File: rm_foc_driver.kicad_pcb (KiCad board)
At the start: 4 copper layers, 70 x 70 mm, 78 parts, among them J1 SWD, J2 TMC4671, J3 UART, J4 TMC4671, J6 Conn_01x02, J8 Conn_01x03, Q1 CSD18540Q5B, Q2 CSD18540Q5B, Q3 CSD18540Q5B, Q4 CSD18540Q5B, Q5 CSD18540Q5B, Q6 CSD18540Q5B, U1 TPS54540, U10 74HC244, U2 RT9013, U3 STM32F401CCUx, U4 AMS1117-5.0, U5 IR2104, U6 INA2180, U7 MT6701, U8 IR2104, U9 IR2104, Y1 Crystal_GND24

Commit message: version 1.1.0-beta
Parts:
- added C19: 47uF, Capacitor_SMD:C_0805_2012Metric, F.Cu at (190.5, 97.0)
- added C20: 1uF, Capacitor_SMD:C_0603_1608Metric, F.Cu at (186.4, 96.9)
- added C21: 1uF, Capacitor_SMD:C_0603_1608Metric, F.Cu at (137.4, 104.4)
- added C23: 47uF, Capacitor_SMD:C_0805_2012Metric, F.Cu at (189.1, 105.7)
- added J5: Conn_01x03, Connector_PinSocket_2.54mm:PinSocket_1x03_P2.54mm_Vertical, F.Cu at (140.2, 121.9)
- added L2: 2.2uH, Inductor_SMD:L_Neosid_Ms42, F.Cu at (183.4, 102.9)
- added R17: 190k, Resistor_SMD:R_0603_1608Metric, F.Cu at (194.7, 103.1)
- added R18: 10k, Resistor_SMD:R_0603_1608Metric, F.Cu at (196.7, 99.5)
- added R19: 10k, Resistor_SMD:R_0603_1608Metric, F.Cu at (194.7, 99.5)
- added R20: 105k, Resistor_SMD:R_0603_1608Metric, F.Cu at (196.7, 103.1)
- C1: value 1uF -> 10nF
- L1: footprint Inductor_SMD:L_7.3x7.3_H4.5 -> Inductor_SMD:L_Neosid_Ms42
- U4: value AMS1117-5.0 -> SY8303; footprint Package_TO_SOT_SMD:SOT-223-3_TabPin2 -> Package_TO_SOT_SMD:TSOT-23-8
- moved C15 31.2 mm to (154.2, 113.3)
- moved U6 30.2 mm to (149.1, 113.5)
- moved C2 18.9 mm to (178.3, 97.0), turned to -90 degrees
- moved R13 16.5 mm to (160.0, 94.5)
- moved R10 16.5 mm to (158.8, 83.4)
- moved Q5 16.3 mm to (145.3, 87.1)
- moved Q6 16.3 mm to (145.5, 79.5)
- moved Q1 16.1 mm to (161.5, 87.1)
- moved Q2 16.1 mm to (161.8, 79.5)
- moved C18 15.1 mm to (143.9, 94.5)
- moved U8 14.0 mm to (160.0, 101.6)
- moved R16 13.8 mm to (148.0, 94.5)
- moved R14 13.7 mm to (162.1, 94.5)
- moved U9 13.5 mm to (146.1, 101.6)
- moved C17 12.7 mm to (158.0, 94.5)
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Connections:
- C1 pad 1: +12V -> Net-(C1-Pad1)
- C1 pad 2: GND -> Net-(C1-Pad2)
- J4 pad 4: /CS2 -> /CS1
- J8 pad 1: /SH_C -> /SH_A
- J8 pad 3: /SH_A -> /SH_C
- U3 pad 14: /CS2 -> /CS1
- U4 pad 1: GND -> Net-(R17-Pad2)
- U4 pad 2: +5V -> Net-(R19-Pad1)
- U4 pad 3: +12V -> GND
- U7 pad 2: /MODE -> +5V
- U7 pad 3: /ADC1 -> unconnected-(U7-Pad3)
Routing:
- net /MODE: track 67.4 -> 0.00 mm, vias 1 -> 0
- net /ADC1: track 35.7 -> 0.00 mm, vias 2 -> 0
- net /CS1: track 33.3 -> 69.0 mm
- net Net-(C18-Pad1): track 13.2 -> 34.0 mm
- net Net-(C17-Pad1): track 33.1 -> 13.1 mm
- net /PWMA: track 28.3 -> 8.46 mm
- net /SL_A: track 66.8 -> 49.6 mm
- net /PWMC: track 8.39 -> 23.5 mm
- net /CS2: track 14.6 -> 0.00 mm
- net GND: track 21.5 -> 7.71 mm, vias 129 -> 37
- net /SO1: track 47.1 -> 35.0 mm, vias 2 -> 1
- net +3.3V: track 116.6 -> 106.9 mm, vias 7 -> 14
- net Net-(R20-Pad2): track 0.00 -> 8.41 mm
- net /SWDIO: track 25.0 -> 16.6 mm
- net /SO2: track 48.5 -> 40.4 mm, vias 2 -> 1
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- added copper zone on B.Cu, net +12V
- added copper zone on F.Cu, net +12V
- added copper zone on In1.Cu, net +12V
- added copper zone on In2.Cu, net +12V
- added copper zone on B.Cu, net +24V
- added copper zone on B.Cu, net +3.3V
- added copper zone on F.Cu, net +3.3V
- added copper zone on In1.Cu, net +3.3V
- added copper zone on In2.Cu, net +3.3V
- added copper zone on B.Cu, net +5V
- added copper zone on F.Cu, net +5V
- added copper zone on In1.Cu, net +5V
- added copper zone on In2.Cu, net +5V
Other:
- board text added: "A"
- board text added: "B"
- board text added: "Z"
- board text removed: "2022/10/3"
- board text removed: "CLK"
- board text removed: "CS2"
- board text removed: "DynamicX"
- board text removed: "MISO"
- board text removed: "MOSI"
- board text removed: "Q2"
- board text removed: "VER3.0"
- board text removed: "cyl0411"

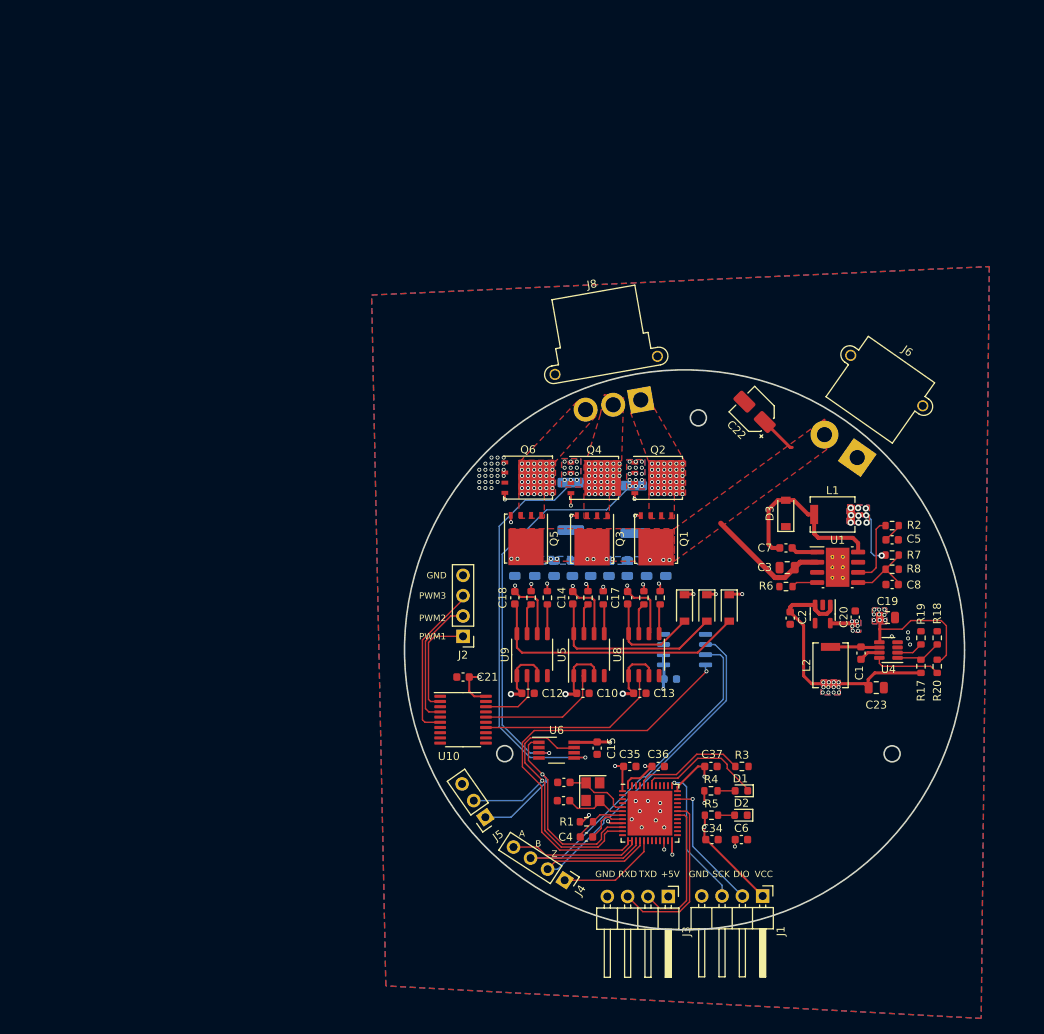
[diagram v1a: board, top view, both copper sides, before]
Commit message: remove mcu...
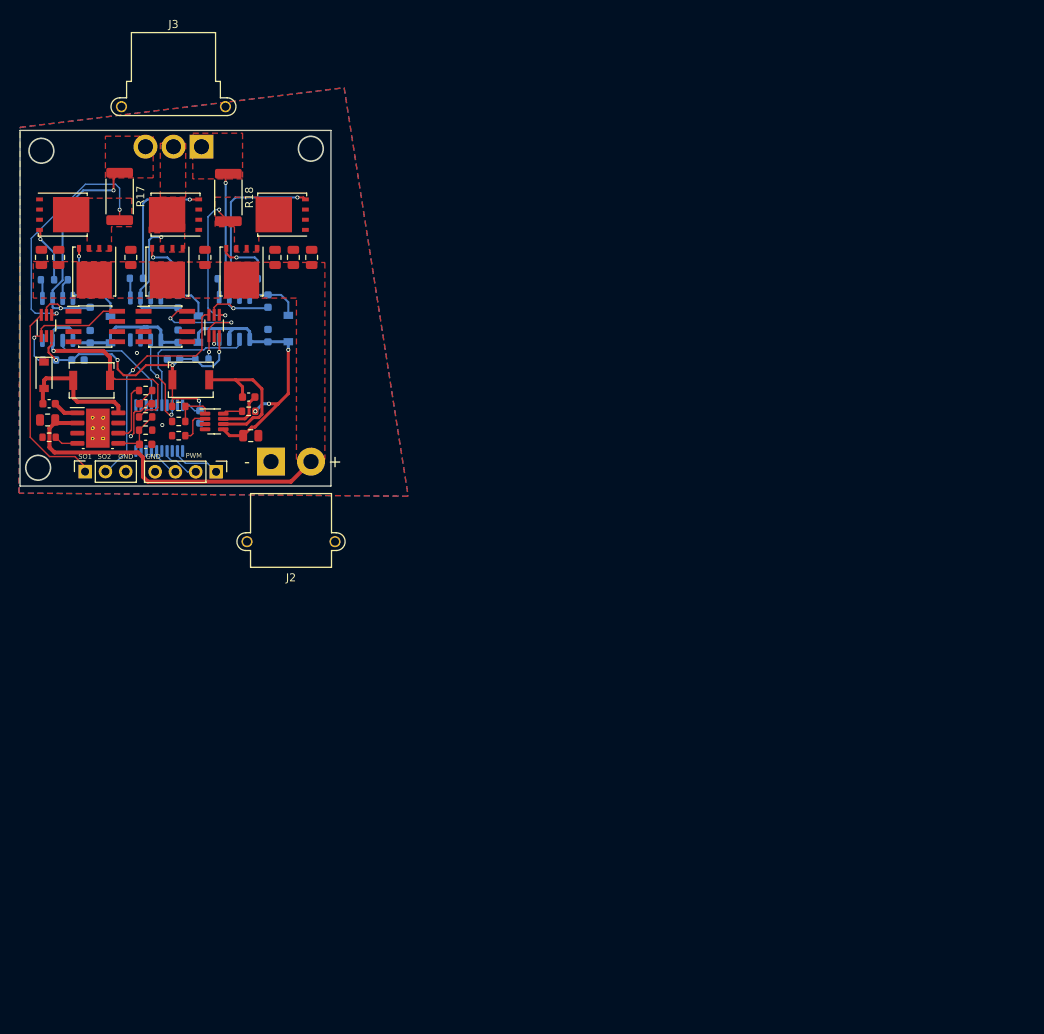
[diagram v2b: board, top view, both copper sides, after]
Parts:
- removed C15: 1uF, Capacitor_SMD:C_0603_1608Metric
- removed C24, C25, C26, C27, C29, C30, C31, C32, C33: 10uF, Capacitor_SMD:C_0805_2012Metric
- removed C34, C35, C36, C37: 100nF, Capacitor_SMD:C_0603_1608Metric
- removed D5, D6: DIODE, Diode_SMD:D_SOD-123
- removed J5: Conn_01x03, Connector_PinSocket_2.54mm:PinSocket_1x03_P2.54mm_Vertical
- removed J6: Conn_01x02, Connector_AMASS:AMASS_XT30PW-M_1x02_P2.50mm_Horizontal
- removed J8: Conn_01x03, Connector_AMASS:AMASS_MR30PW-FB_1x03_P3.50mm_Horizontal
- removed R19: 10k, Resistor_SMD:R_0603_1608Metric
- removed R20: 105k, Resistor_SMD:R_0603_1608Metric
- removed Y1: Crystal_GND24, Crystal:Crystal_SMD_3225-4Pin_3.2x2.5mm
- C1: value 10nF -> 10uF; footprint Capacitor_SMD:C_0603_1608Metric -> Capacitor_SMD:C_0805_2012Metric
- C10, C12, C13, C8, D3, D4, R12, R13, R14, R15, R16, U10, U5: moved to B.Cu
- C11, C9: value 22pF -> 100nF; moved to B.Cu
- C14: value 100nF -> 1uF; moved to B.Cu
- C16: value 1uF -> 10uF; footprint Capacitor_SMD:C_0603_1608Metric -> Capacitor_SMD:C_0805_2012Metric; moved to F.Cu
- C17, C18: value 100nF -> 10uF; footprint Capacitor_SMD:C_0603_1608Metric -> Capacitor_SMD:C_0805_2012Metric
- C19: value 47uF -> 10uF
- C2: value 1uF -> 100nF; moved to B.Cu
- C20, C21: value 1uF -> 10uF; footprint Capacitor_SMD:C_0603_1608Metric -> Capacitor_SMD:C_0805_2012Metric
- C22: value C_Polarized -> 10uF; footprint Capacitor_SMD:CP_Elec_4x5.4 -> Capacitor_SMD:C_0805_2012Metric
- C23: value 47uF -> 100nF; footprint Capacitor_SMD:C_0805_2012Metric -> Capacitor_SMD:C_0603_1608Metric; moved to B.Cu
- C3: value 10uF -> 6.8nF; footprint Capacitor_SMD:C_0805_2012Metric -> Capacitor_SMD:C_0603_1608Metric
- C4: value 100nF -> 10nF
- C5: value 6.8nF -> 100nF
- C6: value 4.7uF -> 47uF; footprint Capacitor_SMD:C_0603_1608Metric -> Capacitor_SMD:C_0805_2012Metric
- D1: value LED -> DIODE; footprint LED_SMD:LED_0603_1608Metric -> Diode_SMD:D_SOD-123
- D2: value LED -> DIODE; footprint LED_SMD:LED_0603_1608Metric -> Diode_SMD:D_SOD-123; moved to B.Cu
- J1: value SWD -> TMC4671; footprint Connector_PinHeader_2.54mm:PinHeader_1x04_P2.54mm_Horizontal -> Connector_PinHeader_2.54mm:PinHeader_1x04_P2.54mm_Vertical
- J2: value TMC4671 -> Conn_01x02; footprint Connector_PinHeader_2.54mm:PinHeader_1x04_P2.54mm_Vertical -> Connector_AMASS:AMASS_XT30PW-M_1x02_P2.50mm_Horizontal
- J3: value UART -> Conn_01x03; footprint Connector_PinHeader_2.54mm:PinHeader_1x04_P2.54mm_Horizontal -> Connector_AMASS:AMASS_MR30PW-FB_1x03_P3.50mm_Horizontal
- J4: value TMC4671 -> Conn_01x03; footprint Connector_PinHeader_2.54mm:PinHeader_1x04_P2.54mm_Vertical -> Connector_PinSocket_2.54mm:PinSocket_1x03_P2.54mm_Vertical
- L1: value 6.5uH -> 2.2uH
- L2: value 2.2uH -> 6.5uH
- R1: value 10k -> 25k
- R10: value 0.01R -> 2.5k; footprint Resistor_SMD:R_2512_6332Metric -> Resistor_SMD:R_0603_1608Metric
- R11: value 0.01R -> 20R; footprint Resistor_SMD:R_2512_6332Metric -> Resistor_SMD:R_0603_1608Metric
- R17: value 190k -> 0.01R; footprint Resistor_SMD:R_0603_1608Metric -> Resistor_SMD:R_2512_6332Metric
- R18: value 10k -> 0.01R; footprint Resistor_SMD:R_0603_1608Metric -> Resistor_SMD:R_2512_6332Metric
- R2: value 25k -> 190k
- R4: value 10k -> 225k
- R6: value 225k -> 105k
- R9: value 20R -> 2.5k; moved to B.Cu
- U2: value RT9013 -> SY8303; footprint Package_TO_SOT_SMD:SOT-23-5 -> Package_TO_SOT_SMD:TSOT-23-8
- U3: value STM32F401CCUx -> IR2104; footprint Package_DFN_QFN:QFN-48-1EP_7x7mm_P0.5mm_EP5.6x5.6mm -> Package_SO:SOP-8_3.9x4.9mm_P1.27mm; moved to B.Cu
- U4: value SY8303 -> IR2104; footprint Package_TO_SOT_SMD:TSOT-23-8 -> Package_SO:SOP-8_3.9x4.9mm_P1.27mm; moved to B.Cu
- U6: value INA2180 -> LM236; footprint Package_SO:VSSOP-8_3.0x3.0mm_P0.65mm -> Package_SO:PowerIntegrations_SO-8
- U7: value MT6701 -> LM236; footprint Package_SO:SOP-8_3.9x4.9mm_P1.27mm -> Package_SO:PowerIntegrations_SO-8; moved to F.Cu
- U8, U9: value IR2104 -> INA199; footprint Package_SO:SOP-8_3.9x4.9mm_P1.27mm -> Package_TO_SOT_SMD:SOT-363_SC-70-6_Handsoldering
- moved R17 116.1 mm to (94.5, 44.3), turned to -90 degrees
- moved U4 111.8 mm to (86.7, 59.7), turned to 90 degrees
- moved J3 110.4 mm to (104.7, 38.1), turned to 0 degrees
- moved C23 107.9 mm to (89.3, 64.8)
- moved C5 106.7 mm to (85.7, 70.2), turned to 180 degrees
- moved C1 105.8 mm to (85.5, 72.3), turned to 180 degrees
- moved R18 104.3 mm to (108.1, 44.5), turned to -90 degrees
- moved D1 101.5 mm to (85.0, 66.7), turned to -90 degrees
- moved L2 99.0 mm to (91.0, 67.3), turned to 0 degrees
- moved C19 96.5 mm to (105.2, 51.9), turned to 90 degrees
- moved R8 94.9 mm to (97.7, 73.5)
- moved R7 94.9 mm to (97.7, 71.9)
- moved U1 94.1 mm to (91.8, 73.3)
- moved R4 93.8 mm to (85.7, 74.4), turned to 180 degrees
- moved C16 92.9 mm to (86.9, 51.9), turned to 90 degrees
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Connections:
- C1 pad 1: Net-(C1-Pad1) -> +24V
- C1 pad 2: Net-(C1-Pad2) -> GND
- C11 pad 1: /OSC_OUT -> Net-(C11-Pad1)
- C11 pad 2: GND -> /SH_B
- C12 pad 1: +12V -> Net-(C12-Pad1)
- C12 pad 2: GND -> /SH_A
- C13 pad 1: +12V -> Net-(C13-Pad1)
- C13 pad 2: GND -> /SH_C
- C14 pad 1: Net-(C14-Pad1) -> +5V
- C14 pad 2: /SH_B -> GND
- C16 pad 1: +5V -> +24V
- C17 pad 1: Net-(C17-Pad1) -> +24V
- C17 pad 2: /SH_A -> GND
- C18 pad 1: Net-(C18-Pad1) -> +24V
- C18 pad 2: /SH_C -> GND
- C19 pad 1: +12V -> +24V
- C20 pad 1: +3.3V -> +24V
- C21 pad 1: +5V -> +24V
- C3 pad 1: +24V -> Net-(C3-Pad1)
- C4 pad 2: GND -> Net-(C4-Pad2)
- C5 pad 2: GND -> Net-(C5-Pad2)
- C6 pad 1: Net-(C6-Pad1) -> +12V
- C7 pad 1: Net-(C7-Pad1) -> GND
- C8 pad 1: GND -> +12V
- C8 pad 2: Net-(C8-Pad2) -> GND
- C9 pad 1: /OSC_IN -> +12V
- D1 pad 1: Net-(D1-Pad1) -> GND
- D1 pad 2: Net-(D1-Pad2) -> Net-(C5-Pad2)
- D2 pad 1: GND -> +12V
- D2 pad 2: Net-(D2-Pad2) -> Net-(C11-Pad1)
- D3 pad 1: GND -> +12V
- D3 pad 2: Net-(C7-Pad2) -> Net-(C12-Pad1)
- D4 pad 2: Net-(C14-Pad1) -> Net-(C13-Pad1)
- J1 pad 1: +3.3V -> /PWM1
- J1 pad 2: /SWDIO -> /PWM2
- J1 pad 3: /SWCLK -> /PWM3
- J2 pad 1: /PWM1 -> GND
- J2 pad 2: /PWM2 -> +24V
- J3 pad 1: +5V -> /SH_B
- J3 pad 2: /TXD -> /SH_C
- J3 pad 3: /RXD -> /SH_A
- J4 pad 1: /MOSI -> /SO1
- J4 pad 2: /MISO -> /SO2
- J4 pad 3: /SCLK -> GND
- L1 pad 1: Net-(C7-Pad2) -> +5V
- L1 pad 2: +12V -> Net-(C4-Pad2)
- L2 pad 1: +5V -> Net-(C5-Pad2)
- L2 pad 2: Net-(C1-Pad2) -> +12V
- Q1 pad 1: /SH_A -> /A_P
- Q1 pad 2: /SH_A -> /A_P
- Q1 pad 3: /SH_A -> /A_P
- Q2 pad 1: /SL_A -> GND
- Q2 pad 2: /SL_A -> GND
- Q2 pad 3: /SL_A -> GND
- Q2 pad 5: /SH_A -> /A_P
- Q3 pad 1: /SH_B -> /B_P
- Q3 pad 2: /SH_B -> /B_P
- Q3 pad 3: /SH_B -> /B_P
- Q4 pad 1: /SL_B -> GND
- Q4 pad 2: /SL_B -> GND
- Q4 pad 3: /SL_B -> GND
- Q4 pad 5: /SH_B -> /B_P
- R1 pad 1: Net-(C4-Pad1) -> Net-(R1-Pad1)
- R1 pad 2: +3.3V -> Net-(C3-Pad1)
- R10 pad 1: /SL_A -> +5V
- R10 pad 2: GND -> Net-(R10-Pad2)
- R11 pad 1: /SL_B -> /GH_B
- R11 pad 2: GND -> Net-(R11-Pad2)
- R17 pad 1: +5V -> /SH_A
- R17 pad 2: Net-(R17-Pad2) -> /A_P
- R18 pad 1: Net-(R17-Pad2) -> /SH_B
- R18 pad 2: GND -> /B_P
- R2 pad 1: Net-(R2-Pad1) -> +5V
- R2 pad 2: Net-(C5-Pad1) -> Net-(R2-Pad2)
- R3 pad 1: Net-(R3-Pad1) -> Net-(R2-Pad2)
- R4 pad 1: +3.3V -> Net-(R4-Pad1)
- R4 pad 2: Net-(D1-Pad2) -> GND
- R5 pad 1: +3.3V -> Net-(R5-Pad1)
- R5 pad 2: Net-(D2-Pad2) -> GND
- R6 pad 1: Net-(R6-Pad1) -> +12V
- R6 pad 2: GND -> Net-(R6-Pad2)
- R7 pad 2: Net-(C8-Pad2) -> Net-(C7-Pad2)
- R8 pad 1: Net-(C8-Pad2) -> Net-(C7-Pad2)
- R9 pad 1: /GH_B -> +5V
- U1 pad 1: Net-(C7-Pad1) -> Net-(C5-Pad1)
- U1 pad 4: Net-(R6-Pad1) -> Net-(R4-Pad1)
- U1 pad 5: Net-(C8-Pad2) -> Net-(C7-Pad2)
- U1 pad 6: Net-(R2-Pad1) -> Net-(R1-Pad1)
- U1 pad 8: Net-(C7-Pad2) -> Net-(C5-Pad2)
- U2 pad 1: +5V -> Net-(R2-Pad2)
- U2 pad 2: GND -> Net-(R5-Pad1)
- U2 pad 3: +5V -> GND
- U2 pad 4: unconnected-(U2-Pad4) -> GND
- U2 pad 5: +3.3V -> +12V
- U3 pad 1: +3.3V -> +12V
- U3 pad 2: unconnected-(U3-Pad2) -> /PWMB
- U3 pad 3: unconnected-(U3-Pad3) -> +12V
- U3 pad 4: unconnected-(U3-Pad4) -> GND
- U3 pad 5: /OSC_IN -> Net-(R12-Pad2)
- U3 pad 6: /OSC_OUT -> /SH_B
- U3 pad 7: Net-(C4-Pad1) -> Net-(R11-Pad2)
- U3 pad 8: GND -> Net-(C11-Pad1)
- U4 pad 1: Net-(R17-Pad2) -> +12V
- U4 pad 2: Net-(R19-Pad1) -> /PWMC
- U4 pad 3: GND -> +12V
- U4 pad 5: +12V -> Net-(R14-Pad2)
- U4 pad 6: Net-(C1-Pad2) -> /SH_A
- U4 pad 7: Net-(C1-Pad1) -> Net-(R13-Pad2)
- U4 pad 8: Net-(R20-Pad2) -> Net-(C12-Pad1)
- U5 pad 2: /PWMB -> /PWMA
- U5 pad 5: Net-(R12-Pad2) -> Net-(R16-Pad2)
- U5 pad 6: /SH_B -> /SH_C
- U5 pad 7: Net-(R9-Pad2) -> Net-(R15-Pad2)
- U5 pad 8: Net-(C14-Pad1) -> Net-(C13-Pad1)
- U6 pad 1: /SO1 -> unconnected-(U6-Pad1)
- U6 pad 2: GND -> unconnected-(U6-Pad2)
- U6 pad 3: /SL_A -> unconnected-(U6-Pad3)
- U6 pad 5: /SL_B -> unconnected-(U6-Pad5)
- U6 pad 6: GND -> unconnected-(U6-Pad6)
- U6 pad 7: /SO2 -> unconnected-(U6-Pad7)
- U6 pad 8: +5V -> Net-(R9-Pad2)
- U7 pad 1: +5V -> unconnected-(U7-Pad1)
- U7 pad 2: +5V -> unconnected-(U7-Pad2)
- U7 pad 6: /MISO -> unconnected-(U7-Pad6)
- U7 pad 7: /SCLK -> unconnected-(U7-Pad7)
- U7 pad 8: /CS1 -> Net-(R10-Pad2)
- U8 pad 1: +12V -> Net-(R9-Pad2)
- U8 pad 2: /PWMC -> GND
- U8 pad 3: +12V -> +5V
- U8 pad 4: GND -> /A_P
- U8 pad 5: Net-(R14-Pad2) -> /SH_A
- U8 pad 6: /SH_A -> /SO1
- U9 pad 1: +12V -> Net-(R10-Pad2)
- U9 pad 2: /PWMA -> GND
- U9 pad 3: +12V -> +5V
- U9 pad 4: GND -> /B_P
- U9 pad 5: Net-(R16-Pad2) -> /SH_B
- U9 pad 6: /SH_C -> /SO2
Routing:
- net +5V: track 151.6 -> 43.0 mm, vias 15 -> 5
- net +3.3V: track 106.9 -> 0.00 mm, vias 14 -> 0
- net /CS1: track 69.0 -> 0.00 mm, vias 1 -> 0
- net /SCLK: track 54.3 -> 0.00 mm
- net /MISO: track 53.5 -> 0.00 mm
- net /SL_B: track 50.1 -> 0.00 mm, vias 13 -> 0
- net /SL_A: track 49.6 -> 0.00 mm, vias 16 -> 0
- net +12V: track 123.0 -> 87.1 mm, vias 25 -> 4
- net Net-(C18-Pad1): track 34.0 -> 0.00 mm
- net /A_P: track 0.00 -> 31.0 mm, vias 0 -> 2
- net Net-(C14-Pad1): track 23.5 -> 0.00 mm
- net +24V: track 20.4 -> 43.6 mm, vias 11 -> 0
- net /RXD: track 21.7 -> 0.00 mm
- net /B_P: track 0.00 -> 18.4 mm, vias 0 -> 2
- net Net-(C4-Pad2): track 0.00 -> 18.1 mm
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- added copper zone on F.Cu, net /A_P
- added copper zone on F.Cu, net /B_P
- removed copper zone on B.Cu, net +12V
- removed copper zone on F.Cu, net +12V
- removed copper zone on In1.Cu, net +12V
- removed copper zone on In2.Cu, net +12V
- removed copper zone on B.Cu, net +24V
- removed copper zone on B.Cu, net +3.3V
- removed copper zone on F.Cu, net +3.3V
- removed copper zone on In1.Cu, net +3.3V
- removed copper zone on In2.Cu, net +3.3V
- removed copper zone on B.Cu, net +5V
- removed copper zone on F.Cu, net +5V
- removed copper zone on In1.Cu, net +5V
- removed copper zone on In2.Cu, net +5V
- removed copper zone on In1.Cu, net /SH_A
- removed copper zone on In2.Cu, net /SH_A
- removed copper zone on In1.Cu, net /SH_B
- removed copper zone on In2.Cu, net /SH_B
- removed copper zone on In1.Cu, net /SH_C
- removed copper zone on In2.Cu, net /SH_C
- removed copper zone on B.Cu, net /SL_A
- removed copper zone on F.Cu, net /SL_A
- removed copper zone on B.Cu, net /SL_B
- removed copper zone on F.Cu, net /SL_B
- removed copper zone on In1.Cu, net GND
- removed copper zone on In2.Cu, net GND
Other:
- board size 70 x 70 mm -> 38.9 x 44.5 mm
- copper layers 4 -> 2
- board text added: "PWM"
- board text added: "SO1"
- board text added: "SO2"
- board text removed: "+5V"
- board text removed: "A"
- board text removed: "B"
- board text removed: "DIO"
- board text removed: "PWM1"
- board text removed: "PWM2"
- board text removed: "PWM3"
- board text removed: "RXD"
- board text removed: "SCK"
- board text removed: "TXD"
- board text removed: "VCC"
- board text removed: "Z"

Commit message: 20230111 AD8418
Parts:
- removed R10, R9: 2.5k, Resistor_SMD:R_0603_1608Metric
- removed U8, U9: INA199, Package_TO_SOT_SMD:SOT-363_SC-70-6_Handsoldering
- U6, U7: value LM236 -> AD8418; footprint Package_SO:PowerIntegrations_SO-8 -> Package_SO:SOP-8_3.9x4.9mm_P1.27mm
- moved U6 17.9 mm to (109.3, 60.7)
- moved U7 8.89 mm to (91.3, 60.7), turned to 180 degrees
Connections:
- U6 pad 1: unconnected-(U6-Pad1) -> /SH_B
- U6 pad 2: unconnected-(U6-Pad2) -> GND
- U6 pad 3: unconnected-(U6-Pad3) -> GND
- U6 pad 4: GND -> unconnected-(U6-Pad4)
- U6 pad 5: unconnected-(U6-Pad5) -> /SO2
- U6 pad 6: unconnected-(U6-Pad6) -> +5V
- U6 pad 7: unconnected-(U6-Pad7) -> +5V
- U6 pad 8: Net-(R9-Pad2) -> /B_P
- U7 pad 1: unconnected-(U7-Pad1) -> /SH_A
- U7 pad 2: unconnected-(U7-Pad2) -> GND
- U7 pad 3: unconnected-(U7-Pad3) -> GND
- U7 pad 4: GND -> unconnected-(U7-Pad4)
- U7 pad 5: unconnected-(U7-Pad5) -> /SO1
- U7 pad 6: unconnected-(U7-Pad6) -> +5V
- U7 pad 7: unconnected-(U7-Pad7) -> +5V
- U7 pad 8: Net-(R10-Pad2) -> /A_P
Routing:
- net Net-(R10-Pad2): track 17.2 -> 0.00 mm, vias 3 -> 0
- net Net-(R9-Pad2): track 15.8 -> 0.00 mm, vias 1 -> 0
- net +5V: track 43.0 -> 51.6 mm, vias 5 -> 4
- net /A_P: track 31.0 -> 36.0 mm
- net /SO1: track 24.9 -> 29.1 mm
- net /B_P: track 18.4 -> 22.0 mm
- net /SO2: track 28.8 -> 32.2 mm
- net /SH_A: track 30.5 -> 33.7 mm
- net /SH_B: track 25.6 -> 24.0 mm
- net GND: vias 4 -> 9
